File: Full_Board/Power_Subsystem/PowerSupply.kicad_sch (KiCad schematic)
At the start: 19 parts, among them IC4 LM2576HVS-5.0_NOPB, J7 KLDHCX-8-0202-A, U1 LM2576SX-3.3-NOPB

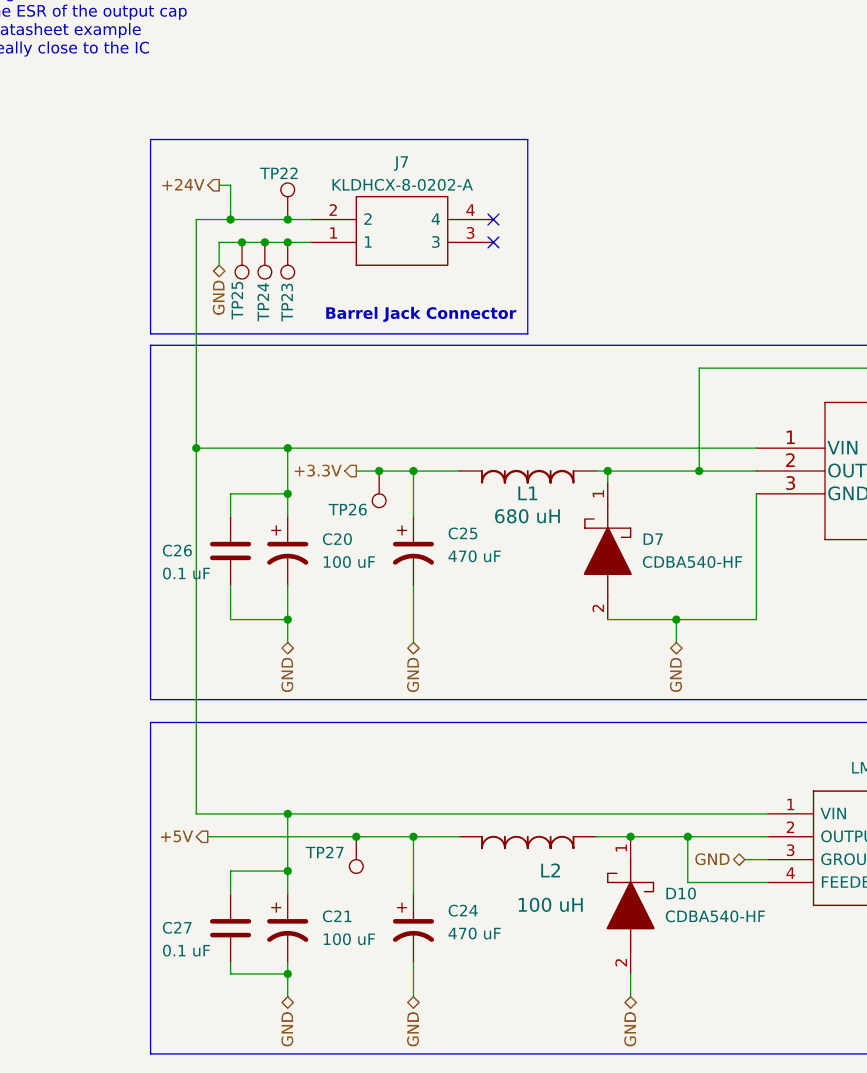
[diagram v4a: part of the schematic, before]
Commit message: Merge Eli and Gabi files. Remove unecessary ECAD remnants. Update stepper components post-part order
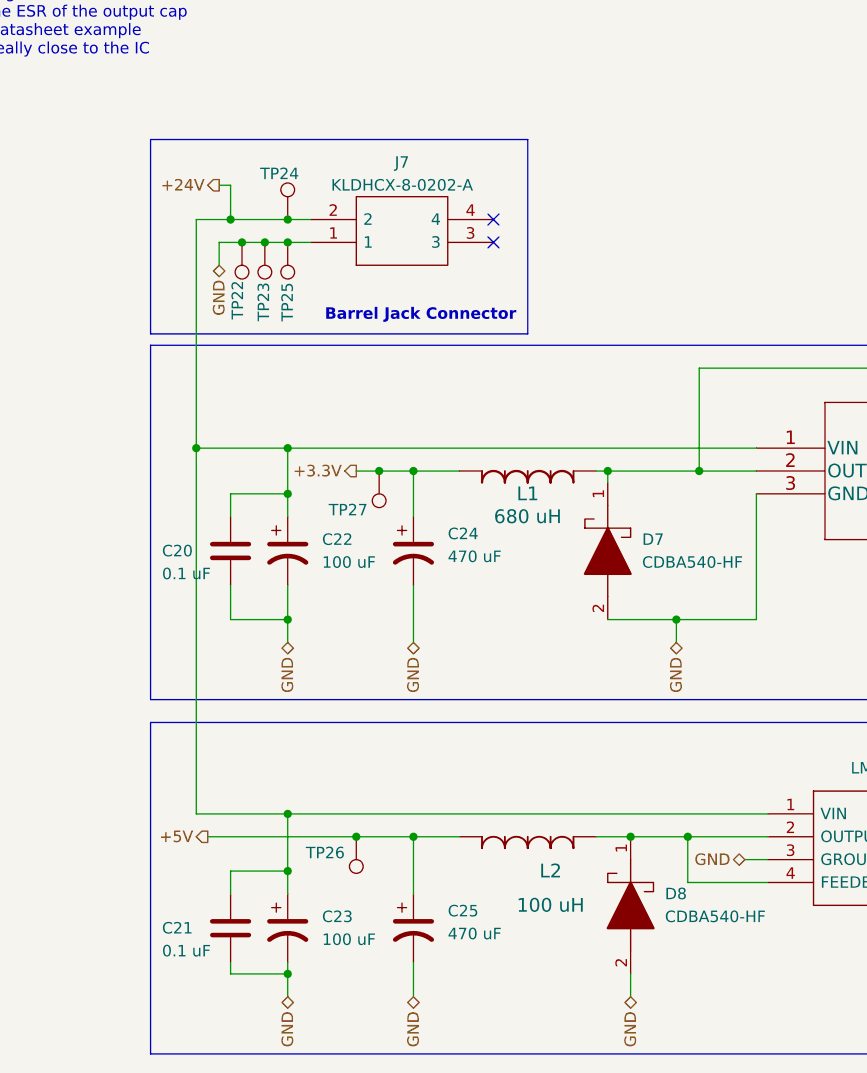
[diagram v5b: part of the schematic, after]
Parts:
- D7: footprint CDBA540-HF:DIOM5225X250N -> DIOM5225X250N
- D8: renamed from D10; footprint CDBA540-HF:DIOM5225X250N -> DIOM5225X250N
- J7: footprint KLDHCX-8-0202-A:KLDHCX80202A -> KLDHCX80202A
- L1: Digikey Link (none) -> https://www.digikey.com/en/products/detail/bourns-inc/SRR12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; Manufacturers Part Number (none) -> SRR1210-681M
- renumbered C26 to C20, C27 to C21, C20 to C22, C21 to C23, C25 to C24, C24 to C25, TP25 to TP22, TP24 to TP23, TP22 to TP24, TP23 to TP25, TP27 to TP26, TP26 to TP27
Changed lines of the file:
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@@
   (symbol (lib_id "Device:C_Polarized_US") (at 109.22 129.54 0) (unit 1)
     (in_bom yes) (on_board yes) (fields_autoplaced)
-    (property "Reference" "C24" (id 0) (at 113.03 127.6349 0)
+    (property "Reference" "C25" (id 0) (at 113.03 127.6349 0)
       (effects (font (size 1.27 1.27)) (justify left))
     )
@@
       (effects (font (size 1.27 1.27)) hide)
     )
-    (property "Datasheet" "https://industrial.panasonic.com/cdbs/www-data/pdf/RDE0000/ABA0000C1184.pdf" (id 3) (at 109.22 129.54 0)
+    (property "Datasheet" "~" (id 3) (at 109.22 129.54 0)
       (effects (font (size 1.27 1.27)) hide)
     )
@@
     (property "Reference" "J7" (id 0) (at 107.95 44.45 0))
     (property "Value" "KLDHCX-8-0202-A" (id 1) (at 107.95 46.99 0))
-    (property "Footprint" "KLDHCX-8-0202-A:KLDHCX80202A" (id 2) (at 114.3 55.88 0)
+    (property "Footprint" "KLDHCX80202A" (id 2) (at 114.3 55.88 0)
       (effects (font (size 1.27 1.27)) (justify left) hide)
     )
@@
   (symbol (lib_id "Connector:TestPoint") (at 95.25 53.34 0) (mirror x) (unit 1)
     (in_bom yes) (on_board yes)
-    (property "Reference" "TP23" (id 0) (at 95.2324 57.7855 90)
+    (property "Reference" "TP25" (id 0) (at 95.2324 57.7855 90)
       (effects (font (size 1.27 1.27)) (justify left))
     )
@@
   (symbol (lib_id "Device:C_Polarized_US") (at 95.25 129.54 0) (unit 1)
     (in_bom yes) (on_board yes)
-    (property "Reference" "C21" (id 0) (at 99.06 128.27 0)
+    (property "Reference" "C23" (id 0) (at 99.06 128.27 0)
       (effects (font (size 1.27 1.27)) (justify left))
     )
@@
       (effects (font (size 1.27 1.27)) hide)
     )
-    (property "Datasheet" "https://www.we-online.com/katalog/datasheet/860020573008.pdf" (id 3) (at 95.25 129.54 0)
+    (property "Datasheet" "~" (id 3) (at 95.25 129.54 0)
       (effects (font (size 1.27 1.27)) hide)
     )
@@
   (symbol (lib_id "Connector:TestPoint") (at 95.25 50.8 0) (mirror y) (unit 1)
     (in_bom yes) (on_board yes)
-    (property "Reference" "TP22" (id 0) (at 96.52 45.72 0)
+    (property "Reference" "TP24" (id 0) (at 96.52 45.72 0)
       (effects (font (size 1.27 1.27)) (justify left))
     )
@@
   (symbol (lib_id "Connector:TestPoint") (at 92.71 53.34 0) (mirror x) (unit 1)
     (in_bom yes) (on_board yes)
-    (property "Reference" "TP24" (id 0) (at 92.5898 57.7656 90)
+    (property "Reference" "TP23" (id 0) (at 92.5898 57.7656 90)
       (effects (font (size 1.27 1.27)) (justify left))
     )
@@
   (symbol (lib_id "Device:C") (at 88.9 129.54 0) (unit 1)
     (in_bom yes) (on_board yes)
-    (property "Reference" "C27" (id 0) (at 81.28 129.54 0)
+    (property "Reference" "C21" (id 0) (at 81.28 129.54 0)
       (effects (font (size 1.27 1.27)) (justify left))
     )
@@
       (effects (font (size 1.27 1.27)) hide)
     )
-    (property "Datasheet" "https://media.digikey.com/pdf/Data%20Sheets/Samsung%20PDFs/CL05A104KP5NNNC_Spec.pdf" (id 3) (at 88.9 129.54 0)
+    (property "Datasheet" "~" (id 3) (at 88.9 129.54 0)
       (effects (font (size 1.27 1.27)) hide)
     )
@@
       (effects (font (size 1.27 1.27)) (justify left))
     )
-    (property "Footprint" "CDBA540-HF:DIOM5225X250N" (id 2) (at 134.62 90.17 0)
+    (property "Footprint" "DIOM5225X250N" (id 2) (at 134.62 90.17 0)
       (effects (font (size 1.27 1.27)) (justify left) hide)
     )
@@
   (symbol (lib_id "Connector:TestPoint") (at 102.87 119.38 180) (unit 1)
     (in_bom yes) (on_board yes)
-    (property "Reference" "TP27" (id 0) (at 101.6 121.92 0)
+    (property "Reference" "TP26" (id 0) (at 101.6 121.92 0)
       (effects (font (size 1.27 1.27)) (justify left top))
     )
@@
   (symbol (lib_id "Device:C") (at 88.9 87.63 0) (unit 1)
     (in_bom yes) (on_board yes)
-    (property "Reference" "C26" (id 0) (at 81.28 87.63 0)
+    (property "Reference" "C20" (id 0) (at 81.28 87.63 0)
       (effects (font (size 1.27 1.27)) (justify left))
     )
@@
       (effects (font (size 1.27 1.27)) hide)
     )
-    (property "Datasheet" "https://media.digikey.com/pdf/Data%20Sheets/Samsung%20PDFs/CL05A104KP5NNNC_Spec.pdf" (id 3) (at 88.9 87.63 0)
+    (property "Datasheet" "~" (id 3) (at 88.9 87.63 0)
       (effects (font (size 1.27 1.27)) hide)
     )
@@
   (symbol (lib_id "Device:C_Polarized_US") (at 95.25 87.63 0) (unit 1)
     (in_bom yes) (on_board yes)
-    (property "Reference" "C20" (id 0) (at 99.06 86.36 0)
+    (property "Reference" "C22" (id 0) (at 99.06 86.36 0)
       (effects (font (size 1.27 1.27)) (justify left))
     )
@@
       (effects (font (size 1.27 1.27)) hide)
     )
-    (property "Datasheet" "https://www.we-online.com/katalog/datasheet/860020573008.pdf" (id 3) (at 95.25 87.63 0)
+    (property "Datasheet" "~" (id 3) (at 95.25 87.63 0)
       (effects (font (size 1.27 1.27)) hide)
     )
@@
       (effects (font (size 1.27 1.27)) hide)
     )
+    (property "Digikey Link" "https://www.digikey.com/en/products/detail/bourns-inc/SRR1210-681M/2562365" (id 11) (at 129.54 78.74 0)
+      (effects (font (size 1.27 1.27)) hide)
+    )
+    (property "Manufacturers Part Number" "SRR1210-681M" (id 12) (at 129.54 78.74 0)
+      (effects (font (size 1.27 1.27)) hide)
+    )
     (pin "1")
     (pin "2")
@@
   (symbol (lib_id "CDBA540-HF:CDBA540-HF") (at 133.35 116.84 270) (unit 1)
     (in_bom yes) (on_board yes) (fields_autoplaced)
-    (property "Reference" "D10" (id 0) (at 137.16 125.7299 90)
+    (property "Reference" "D8" (id 0) (at 137.16 125.7299 90)
       (effects (font (size 1.27 1.27)) (justify left))
     )
@@
       (effects (font (size 1.27 1.27)) (justify left))
     )
-    (property "Footprint" "CDBA540-HF:DIOM5225X250N" (id 2) (at 137.16 129.54 0)
+    (property "Footprint" "DIOM5225X250N" (id 2) (at 137.16 129.54 0)
       (effects (font (size 1.27 1.27)) (justify left) hide)
     )
@@
   (symbol (lib_id "Connector:TestPoint") (at 105.41 78.74 180) (unit 1)
     (in_bom yes) (on_board yes)
-    (property "Reference" "TP26" (id 0) (at 104.14 83.82 0)
+    (property "Reference" "TP27" (id 0) (at 104.14 83.82 0)
       (effects (font (size 1.27 1.27)) (justify left top))
     )
@@
   (symbol (lib_id "Connector:TestPoint") (at 90.17 53.34 0) (mirror x) (unit 1)
     (in_bom yes) (on_board yes)
-    (property "Reference" "TP25" (id 0) (at 88.9541 57.567 90)
+    (property "Reference" "TP22" (id 0) (at 88.9541 57.567 90)
       (effects (font (size 1.27 1.27)) (justify left top))
     )
@@
   (symbol (lib_id "Device:C_Polarized_US") (at 109.22 87.63 0) (unit 1)
     (in_bom yes) (on_board yes) (fields_autoplaced)
-    (property "Reference" "C25" (id 0) (at 113.03 85.7249 0)
+    (property "Reference" "C24" (id 0) (at 113.03 85.7249 0)
       (effects (font (size 1.27 1.27)) (justify left))
     )
@@
       (effects (font (size 1.27 1.27)) hide)
     )
-    (property "Datasheet" "https://industrial.panasonic.com/cdbs/www-data/pdf/RDE0000/ABA0000C1184.pdf" (id 3) (at 109.22 87.63 0)
-      (effects (font (size 1.27 1.27)) hide)
-    )
+    (property "Datasheet" "~" (id 3) (at 109.22 87.63 0)
+      (effects (font (size 1.27 1.27)) hide)
+    )

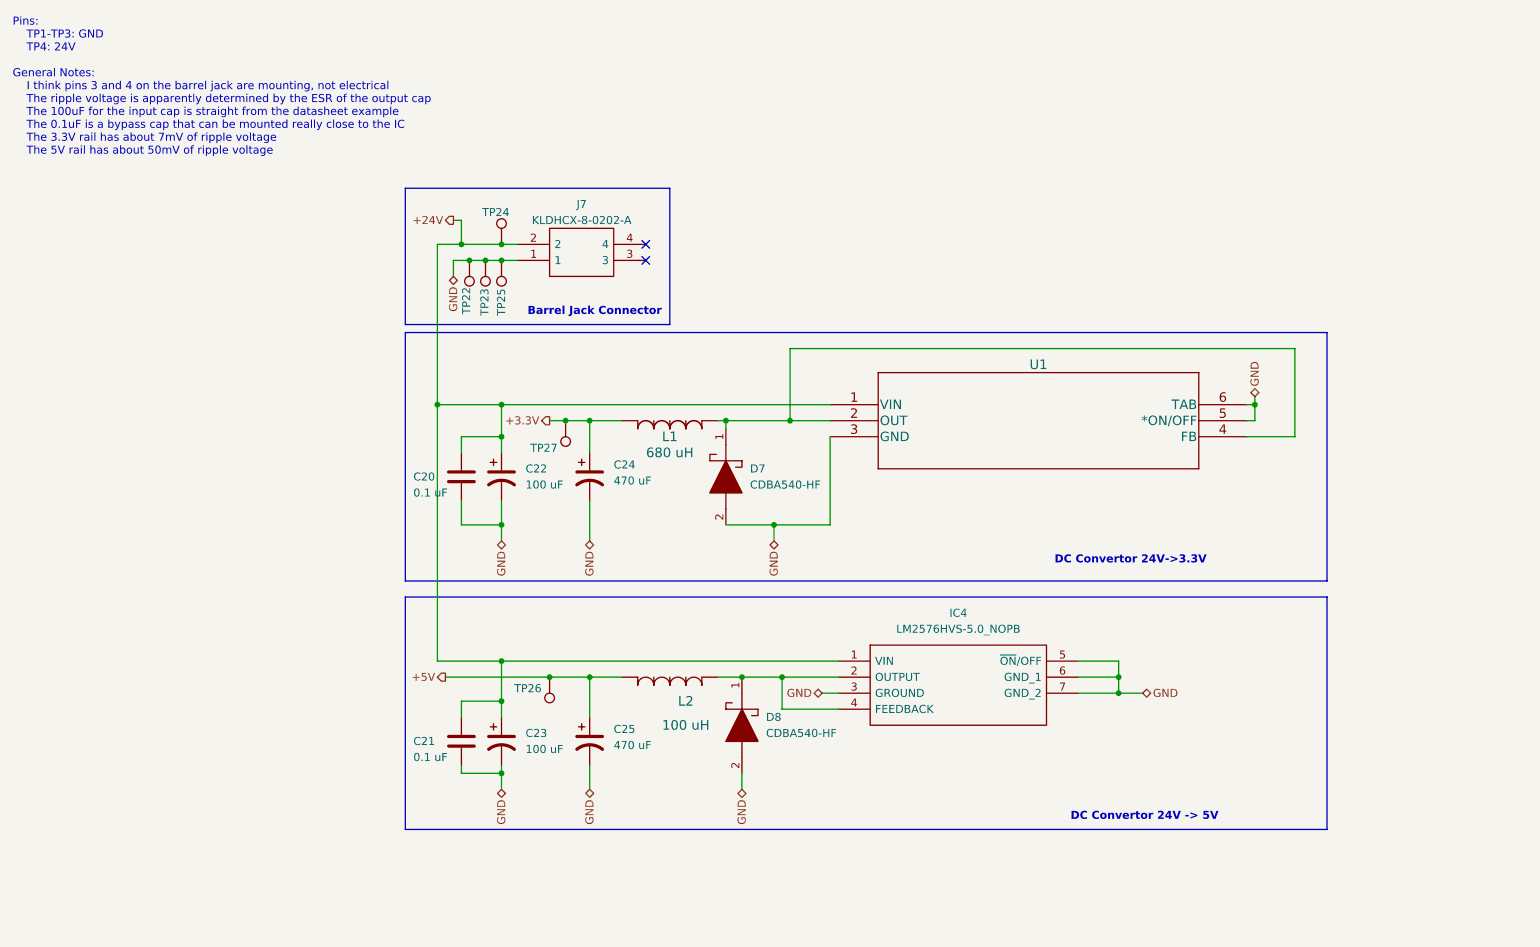
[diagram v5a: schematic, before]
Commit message: Added a fuse and fixed ERC
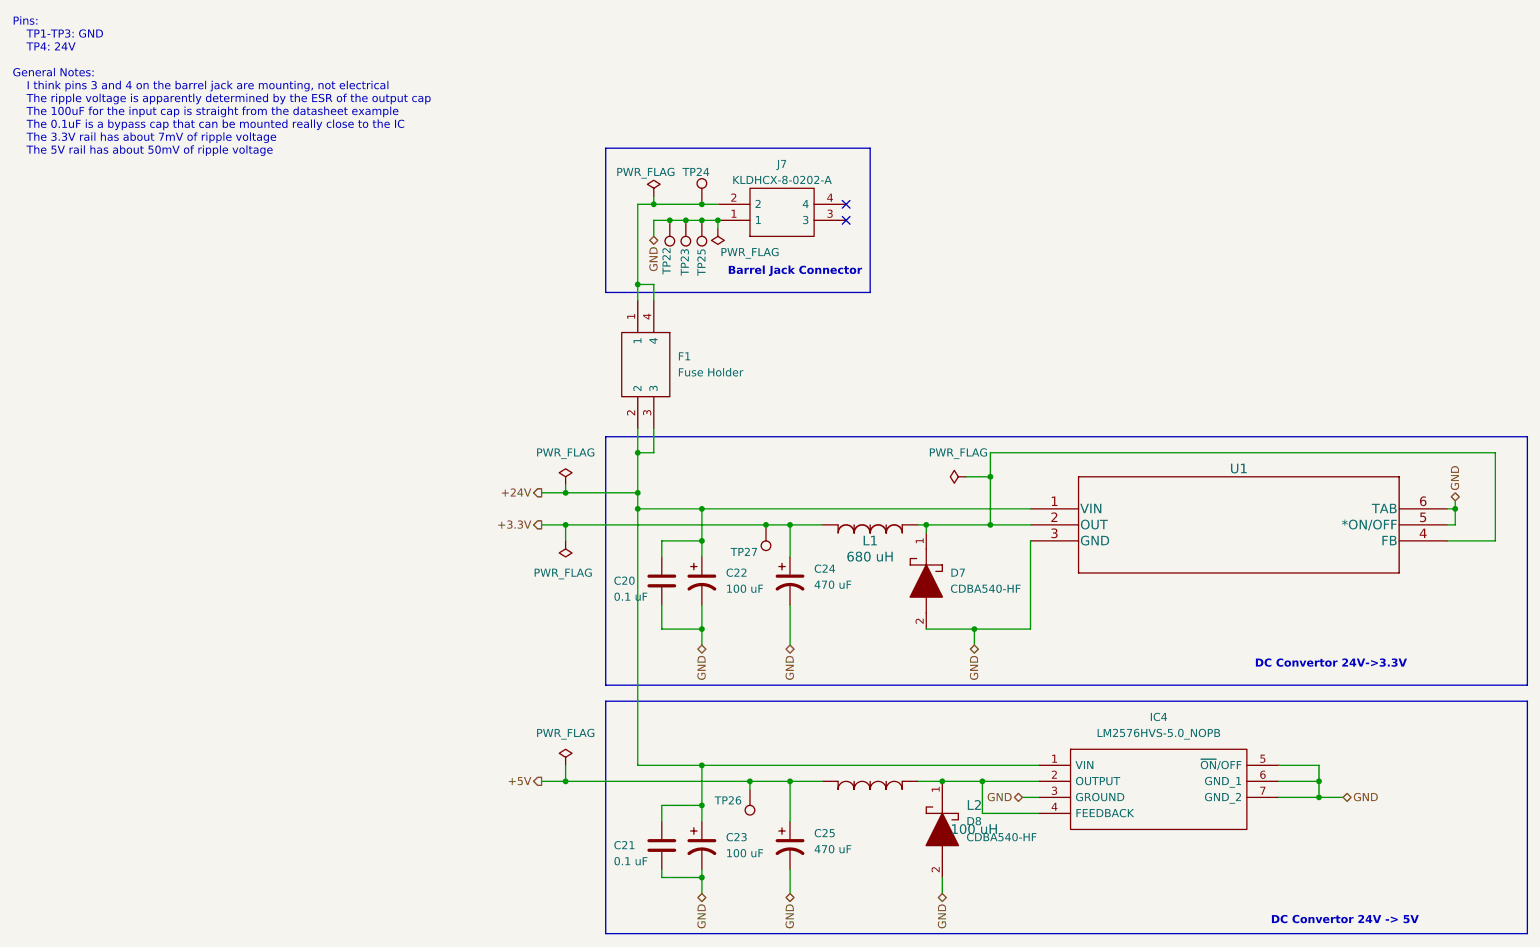
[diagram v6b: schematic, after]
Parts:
- added F1: Fuse Holder, 3588:3588, symbol 3588:3588
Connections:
- net +24V: now also F1.2, F1.3; no longer J7.2, TP24.1
- new net: F1.1, F1.4, J7.2, TP24.1
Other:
- moved on the sheet: C20, C21, C22, C23, C24, C25, D7, D8, IC4, J7, L1, L2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
